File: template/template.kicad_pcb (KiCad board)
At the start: 2 copper layers, 75 x 55 mm, 41 parts, among them J1 Network Connector, J2 B2B STLink connector, SW1 SW_Push, U1 LD39050PU33R, U2 STM32G474RBT6, U3 SN65HVD230, Y1 8MHz

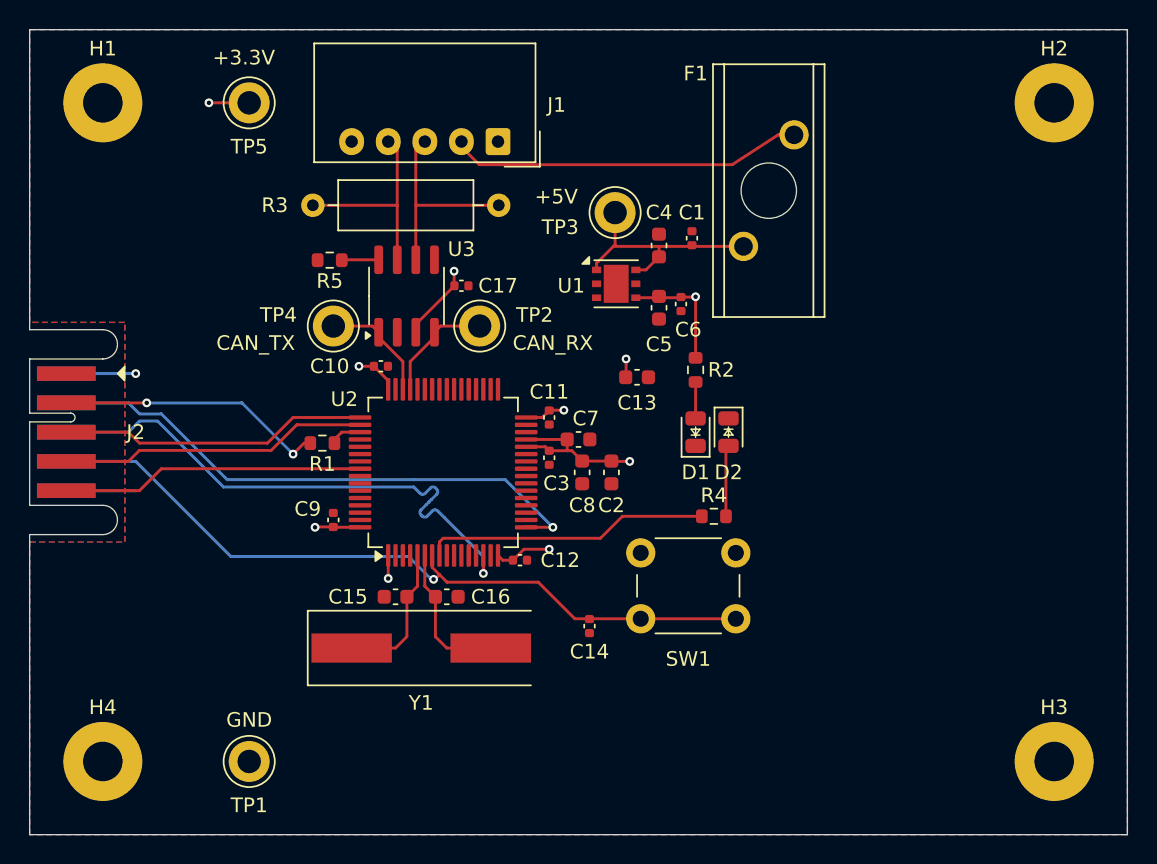
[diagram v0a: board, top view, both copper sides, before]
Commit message: Change B2B connector to STDC14 connector
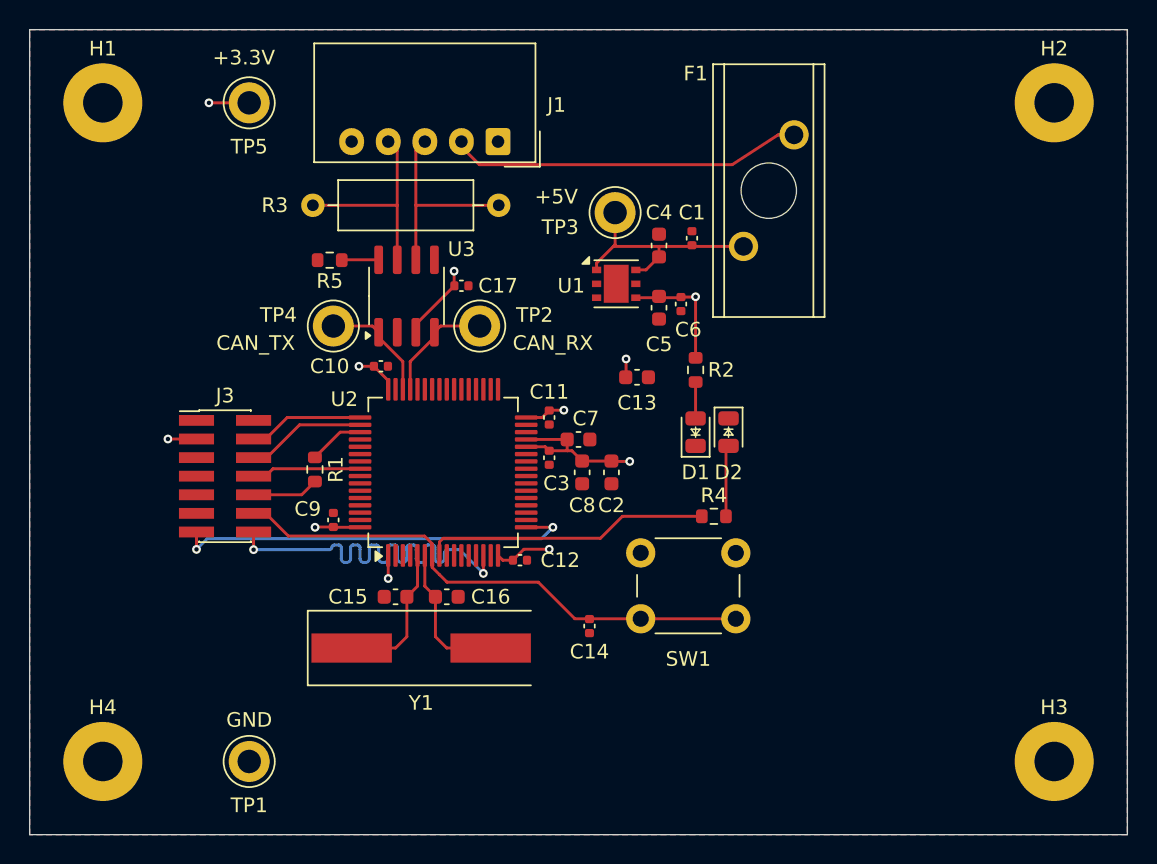
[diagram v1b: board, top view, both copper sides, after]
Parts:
- removed J2: B2B STLink connector, Exocet:AVX 00-9159-010-BTB Connector
- added J3: B2B STLink connector, Connector_PinHeader_1.27mm:PinHeader_2x07_P1.27mm_Vertical_SMD, F.Cu at (203.3, 52.0)
- moved R1 1.87 mm to (209.5, 51.5), turned to -90 degrees
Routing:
- net /STM32 Base Layout/T_NRST: track 52.0 -> 36.9 mm, vias 1 -> 0
- net /STM32 Base Layout/T_JTDI: track 18.4 -> 4.56 mm, vias 2 -> 0
- net /STM32 Base Layout/T_JTMS/T_SWDIO: track 21.1 -> 7.88 mm
- net /STM32 Base Layout/T_JTDO/T_SWO: track 20.7 -> 7.49 mm
- net /STM32 Base Layout/T_JCLK/T_SWCLK: track 21.1 -> 8.20 mm
- net /STM32 Base Layout/T_VCP_RX: track 38.6 -> 28.0 mm, vias 1 -> 2
- net /STM32 Base Layout/T_VCP_TX: track 38.3 -> 30.6 mm, vias 1 -> 2
- net GND: track 4.75 -> 0.00 mm, vias 1 -> 0
- net +3.3V: track 48.0 -> 45.2 mm, vias 10 -> 11
- net Net-(U2-PA15): track 2.21 -> 3.80 mm
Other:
- outline, holes or cut-outs redrawn

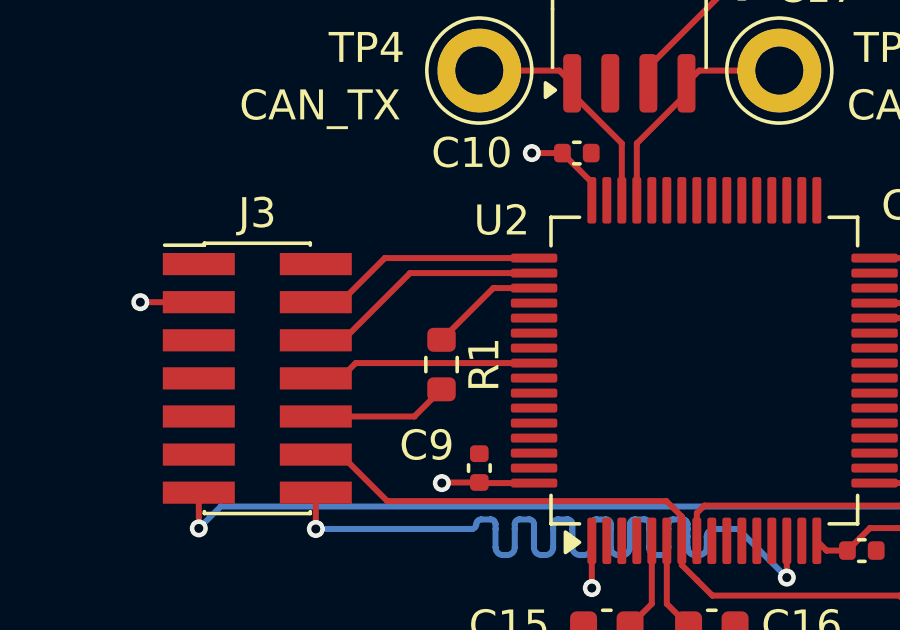
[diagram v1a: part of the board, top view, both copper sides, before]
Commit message: Connect BOOT0 to GND through 10k resistor
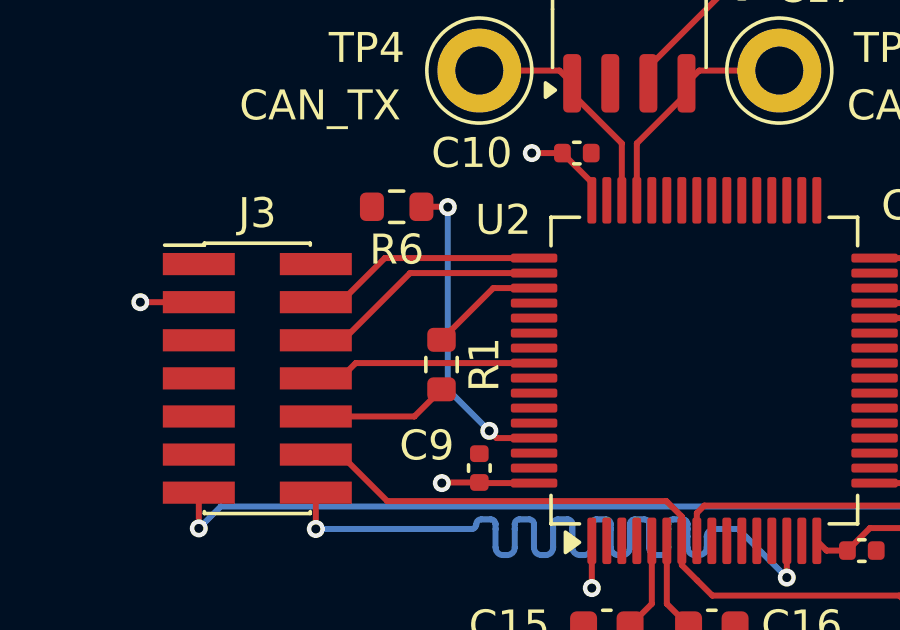
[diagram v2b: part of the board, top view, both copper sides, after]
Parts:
- added R6: 10k, Resistor_SMD:R_0603_1608Metric, F.Cu at (208.0, 46.3)
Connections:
- U2 pad 61: unconnected-(U2-PB8-Pad61) -> Net-(U2-PB8)
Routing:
- net Net-(U2-PB8): track 0.00 -> 10.5 mm, vias 0 -> 2

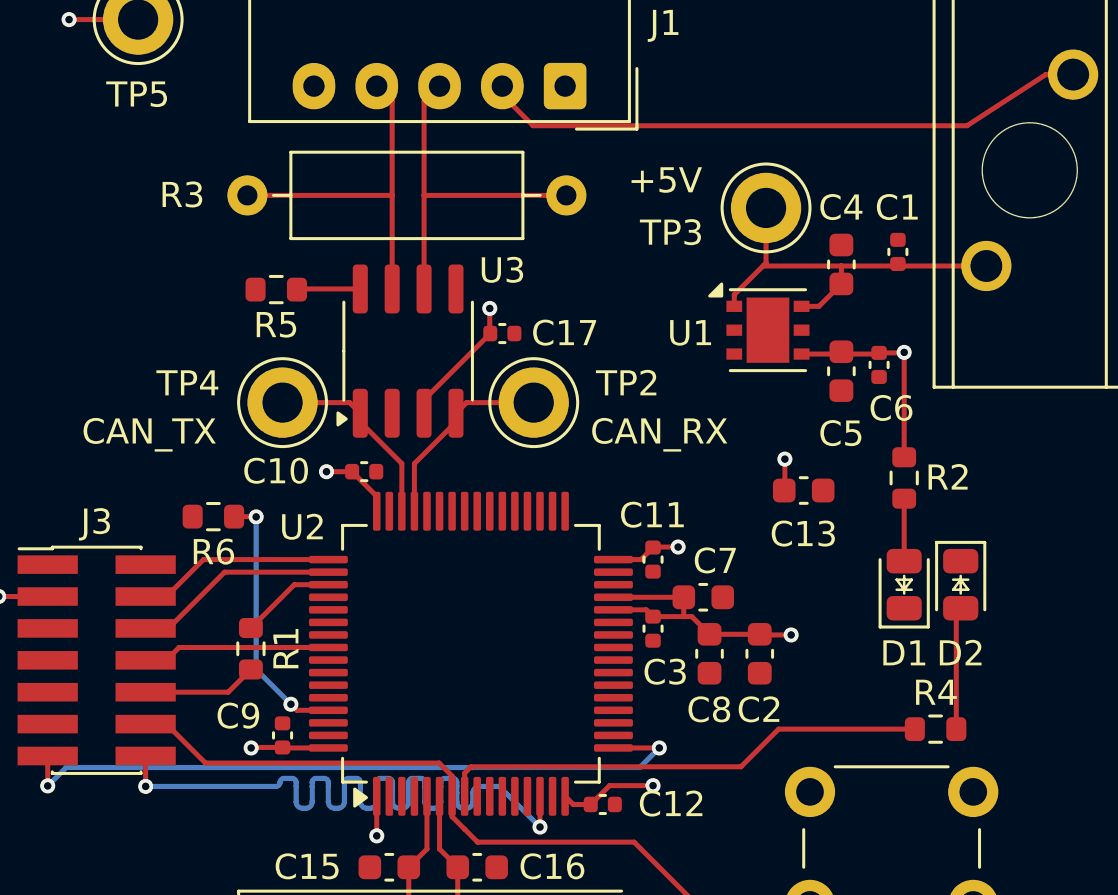
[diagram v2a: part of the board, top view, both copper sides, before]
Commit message: Remove CAN Resistor and change the values of the LED resistors
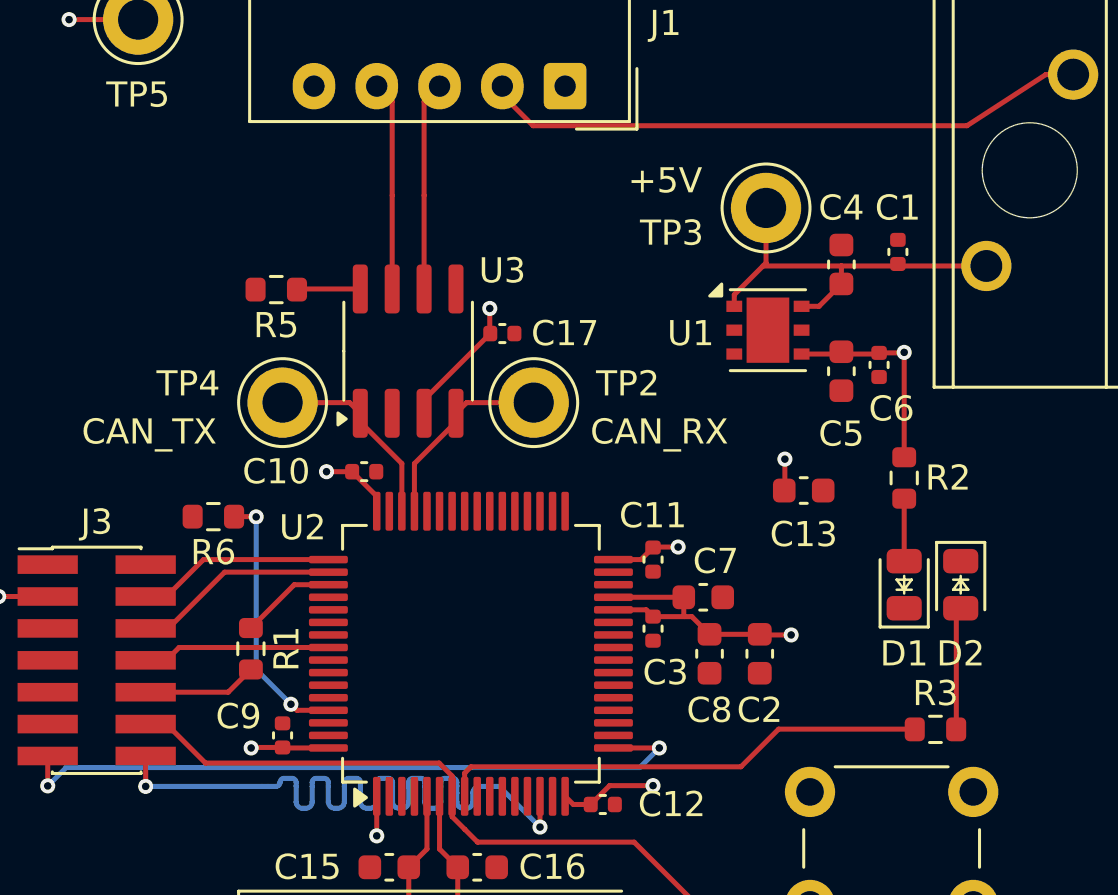
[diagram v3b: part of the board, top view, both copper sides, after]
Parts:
- removed R4: 75, Resistor_SMD:R_0603_1608Metric
- J3: value B2B STLink connector -> STDC14 STLink connector
- R2: value 33 -> 100
- R3: value 120 -> 100; footprint Resistor_THT:R_Axial_DIN0309_L9.0mm_D3.2mm_P12.70mm_Horizontal -> Resistor_SMD:R_0603_1608Metric
- moved R3 25.8 mm to (236.7, 54.8), turned to 0 degrees
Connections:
- R3 pad 1: /STM32 Base Layout/CAN_L -> /STM32 Base Layout/STATUS_LED
- R3 pad 2: /STM32 Base Layout/CAN_H -> Net-(D2-A)
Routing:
- net /STM32 Base Layout/CAN_H: track 14.1 -> 8.33 mm
- net /STM32 Base Layout/CAN_L: track 14.0 -> 8.33 mm
